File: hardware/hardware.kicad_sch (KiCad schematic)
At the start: 17 parts, among them J1 Screw_Terminal_01x02, J2 Screw_Terminal_01x02, J3 Screw_Terminal_01x02, K1 RM85-2011-35-1005, K2 RM85-2011-35-1005, Q1 BC337, Q2 BC337, U1 XIAO-ESP32-C6

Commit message: Updated screw terminals
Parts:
- J1, J2, J3: footprint Degson Electronics:DG1285002P14 -> Degson Electronics:SHDR2W100P0X500_1X2_1000X780X1020P
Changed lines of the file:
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@@
 			)
 		)
-		(property "Footprint" "Degson Electronics:DG1285002P14"
+		(property "Footprint" "Degson Electronics:SHDR2W100P0X500_1X2_1000X780X1020P"
 			(at 185.42 73.66 0)
 			(effects
@@
 			)
 		)
-		(property "Footprint" "Degson Electronics:DG1285002P14"
+		(property "Footprint" "Degson Electronics:SHDR2W100P0X500_1X2_1000X780X1020P"
 			(at 185.42 60.96 0)
 			(effects
@@
 			)
 		)
-		(property "Footprint" "Degson Electronics:DG1285002P14"
+		(property "Footprint" "Degson Electronics:SHDR2W100P0X500_1X2_1000X780X1020P"
 			(at 185.42 86.36 0)
 			(effects

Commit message: Finished PCB layout and traces
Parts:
- PS1: footprint IRM0312 -> Mean Well:IRM0312
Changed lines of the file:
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@@
 			)
 		)
-		(property "Footprint" "IRM0312"
+		(property "Footprint" "Mean Well:IRM0312"
 			(at 193.04 127.94 0)
 			(effects

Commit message: Added headers for extra gpios
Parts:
- added J4, J5: Conn_01x08_Pin, Connector_PinHeader_2.54mm:PinHeader_1x08_P2.54mm_Vertical, symbol Connector:Conn_01x08_Pin
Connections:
- net +3V3: now also J4.7 (Pin_7), J5.7 (Pin_7)
- net +5V: now also J4.8 (Pin_8), J5.8 (Pin_8)
- net GND: now also J4.1 (Pin_1), J4.6 (Pin_6), J5.1 (Pin_1)
- net IO07: now reaches U1.10 (GPIO20/D9/MISO)
- net IO07: now also J4.4 (Pin_4)
- net IO06: now reaches U1.11 (GPIO18/D10/MOSI)
- net IO06: now also J4.5 (Pin_5)
- net IO01: now reaches U1.3 (GPIO2/A2/D2)
- net IO01: now also J5.6 (Pin_6)
- net IO02: now reaches U1.4 (GPIO21/D3)
- net IO02: now also J5.5 (Pin_5)
- net IO03: now reaches U1.5 (GPIO22/D4/SDA)
- net IO03: now also J5.4 (Pin_4)
- net IO04: now reaches U1.6 (GPIO23/D5/SCL)
- net IO04: now also J5.3 (Pin_3)
- net IO05: now reaches U1.7 (GPIO16/D6/TX)
- net IO05: now also J5.2 (Pin_2)
- net IO09: now reaches U1.8 (GPIO17/D7/RX)
- net IO09: now also J4.2 (Pin_2)
- net IO08: now reaches U1.9 (GPIO19/D8/SCK)
- net IO08: now also J4.3 (Pin_3)
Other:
- moved on the sheet: H1, H2

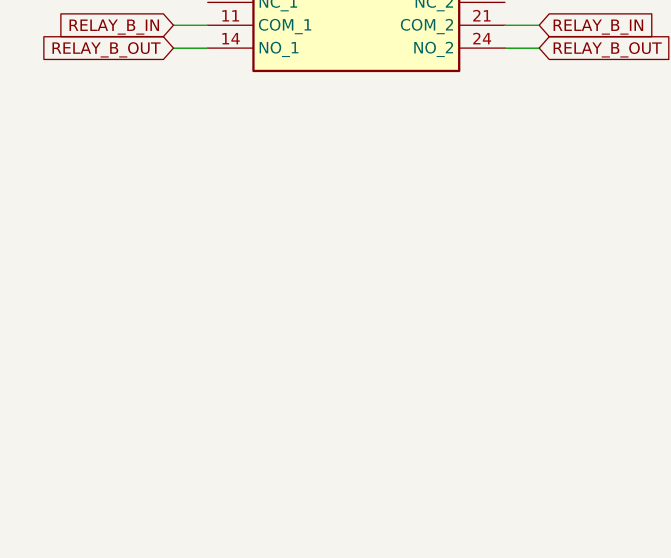
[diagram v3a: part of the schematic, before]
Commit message: Added status LEDs
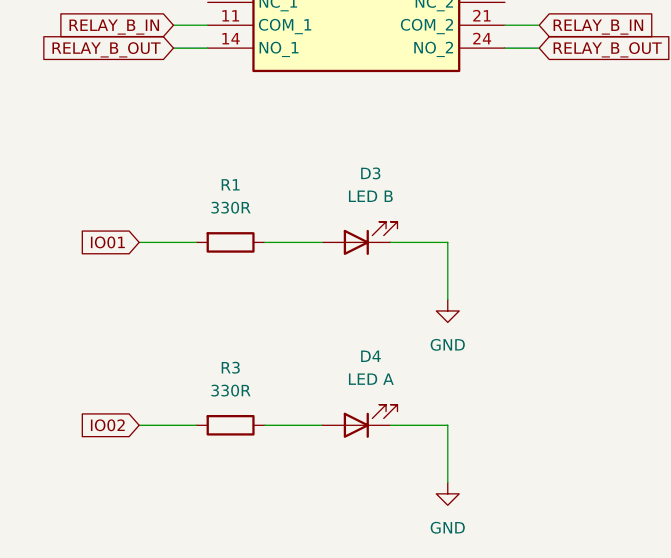
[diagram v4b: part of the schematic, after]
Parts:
- added D3: LED B, LED_THT:LED_D3.0mm, symbol Device:LED
- added D4: LED A, LED_THT:LED_D3.0mm, symbol Device:LED
- added R1, R3: 330R, Resistor_THT:R_Axial_DIN0204_L3.6mm_D1.6mm_P7.62mm_Horizontal, symbol Device:R
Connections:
- net GND: now also D3.1 (K), D4.1 (K)
- net IO01: now also R1.2
- net IO02: now also R3.2
- new net: D3.2 (A), R1.1
- new net: D4.2 (A), R3.1
